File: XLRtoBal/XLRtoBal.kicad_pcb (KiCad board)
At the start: 2 copper layers, 53 parts, among them J1 XLR3, J10 Conn_Coaxial, J11 Conn_Coaxial, J2 Conn_01x04, J3 Conn_01x04, J4 XLR3, J5 Conn_01x04, J6 Conn_01x01, J7 Conn_01x01, J8 Conn_01x01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

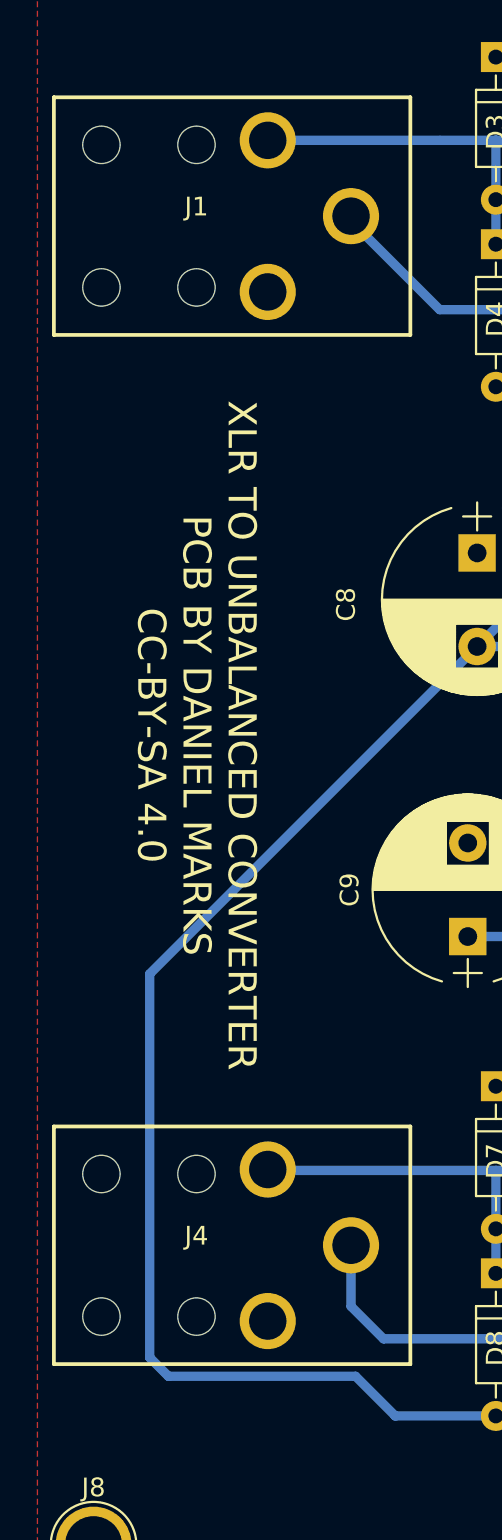
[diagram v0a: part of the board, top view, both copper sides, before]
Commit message: Fixed XLR footprint
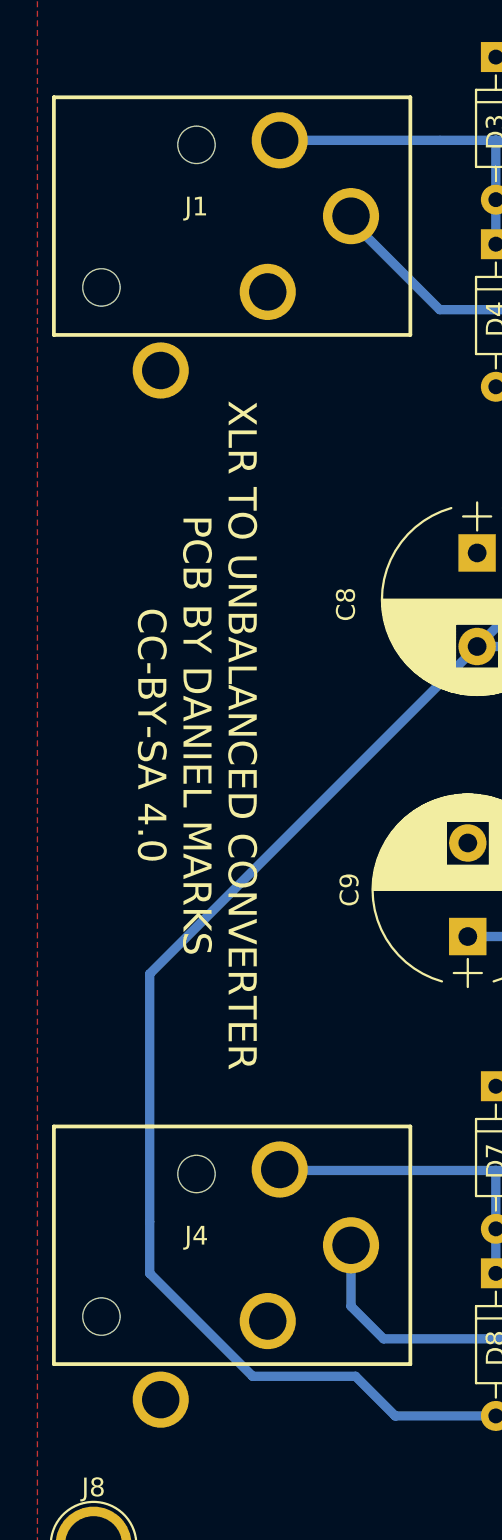
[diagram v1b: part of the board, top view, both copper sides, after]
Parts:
- J1, J4: footprint XLRtoBal:XLR04WP -> XLRtoBal:IOXLR3FEH
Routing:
- net VEE: track 177.5 -> 174.9 mm
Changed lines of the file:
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@@
     (thickness 1.6)
     (drawings 17)
-    (tracks 216)
+    (tracks 217)
     (zones 0)
     (modules 53)
@@
     (pad_to_mask_clearance 0.2)
     (aux_axis_origin 0 0)
-    (visible_elements FFFFFF7F)
+    (visible_elements 7FFFFFFF)
     (pcbplotparams
       (layerselection 0x00030_80000001)
@@
     )
   )
-  (module XLRtoBal:XLR04WP (layer F.Cu)
-    (at 110.5 78 180)
-    (fp_text reference J1 (at 0 0.5 180) (layer F.SilkS)
-      (effects (font (size 1 1) (thickness 0.15)))
-    )
-    (fp_text value XLR3 (at 0 -0.5 180) (layer F.Fab)
-      (effects (font (size 1 1) (thickness 0.15)))
-    )
-    (fp_line (start 7.62 -6.35) (end -11.43 -6.35) (layer F.SilkS) (width 0.2))
-    (fp_line (start -11.43 -6.35) (end -11.43 6.35) (layer F.SilkS) (width 0.2))
-    (fp_line (start -11.43 6.35) (end 7.62 6.35) (layer F.SilkS) (width 0.2))
-    (fp_line (start 7.62 6.35) (end 7.62 -6.35) (layer F.SilkS) (width 0.2))
-    (pad 3 thru_hole circle (at -8.26 0 180) (size 3 3) (drill 2) (layers *.Cu *.Mask)
-      (net 9 "Net-(D1-Pad2)"))
-    (pad 1 thru_hole circle (at -3.81 -4.05 180) (size 3 3) (drill 2) (layers *.Cu *.Mask)
-      (net 4 GND))
-    (pad "" np_thru_hole circle (at 0 -3.81 180) (size 2 2) (drill 2) (layers *.Cu *.Mask))
-    (pad "" np_thru_hole circle (at 5.08 3.81 180) (size 2 2) (drill 2) (layers *.Cu *.Mask))
-    (pad "" np_thru_hole circle (at 5.08 -3.81 180) (size 2 2) (drill 2) (layers *.Cu *.Mask))
-    (pad "" np_thru_hole circle (at 0 3.81 180) (size 2 2) (drill 2) (layers *.Cu *.Mask))
-    (pad 2 thru_hole circle (at -3.81 4.05 180) (size 3 3) (drill 2) (layers *.Cu *.Mask)
-      (net 12 "Net-(D3-Pad2)"))
-  )
   (module Connectors_Terminal_Blocks:TerminalBlock_bornier-4_P5.08mm (layer F.Cu)
     (at 176 62 270)
@@
       (rotate (xyz 0 0 0))
     )
-  )
-  (module XLRtoBal:XLR04WP (layer F.Cu)
-    (at 110.5 133 180)
-    (fp_text reference J4 (at 0 0.5 180) (layer F.SilkS)
-      (effects (font (size 1 1) (thickness 0.15)))
-    )
-    (fp_text value XLR3 (at 0 -0.5 180) (layer F.Fab)
-      (effects (font (size 1 1) (thickness 0.15)))
-    )
-    (fp_line (start 7.62 -6.35) (end -11.43 -6.35) (layer F.SilkS) (width 0.2))
-    (fp_line (start -11.43 -6.35) (end -11.43 6.35) (layer F.SilkS) (width 0.2))
-    (fp_line (start -11.43 6.35) (end 7.62 6.35) (layer F.SilkS) (width 0.2))
-    (fp_line (start 7.62 6.35) (end 7.62 -6.35) (layer F.SilkS) (width 0.2))
-    (pad 3 thru_hole circle (at -8.26 0 180) (size 3 3) (drill 2) (layers *.Cu *.Mask)
-      (net 21 "Net-(D10-Pad1)"))
-    (pad 1 thru_hole circle (at -3.81 -4.05 180) (size 3 3) (drill 2) (layers *.Cu *.Mask)
-      (net 4 GND))
-    (pad "" np_thru_hole circle (at 0 -3.81 180) (size 2 2) (drill 2) (layers *.Cu *.Mask))
-    (pad "" np_thru_hole circle (at 5.08 3.81 180) (size 2 2) (drill 2) (layers *.Cu *.Mask))
-    (pad "" np_thru_hole circle (at 5.08 -3.81 180) (size 2 2) (drill 2) (layers *.Cu *.Mask))
-    (pad "" np_thru_hole circle (at 0 3.81 180) (size 2 2) (drill 2) (layers *.Cu *.Mask))
-    (pad 2 thru_hole circle (at -3.81 4.05 180) (size 3 3) (drill 2) (layers *.Cu *.Mask)
-      (net 20 "Net-(D7-Pad2)"))
   )
   (module Connectors_Terminal_Blocks:TerminalBlock_bornier-4_P5.08mm (layer F.Cu)
@@
       (net 23 "Net-(J11-Pad1)"))
   )
+  (module XLRtoBal:IOXLR3FEH (layer F.Cu)
+    (at 110.5 78 180)
+    (fp_text reference J1 (at 0 0.5 180) (layer F.SilkS)
+      (effects (font (size 1 1) (thickness 0.15)))
+    )
+    (fp_text value XLR3 (at 0 -0.5 180) (layer F.Fab)
+      (effects (font (size 1 1) (thickness 0.15)))
+    )
+    (fp_line (start 7.62 -6.35) (end -11.43 -6.35) (layer F.SilkS) (width 0.2))
+    (fp_line (start -11.43 -6.35) (end -11.43 6.35) (layer F.SilkS) (width 0.2))
+    (fp_line (start -11.43 6.35) (end 7.62 6.35) (layer F.SilkS) (width 0.2))
+    (fp_line (start 7.62 6.35) (end 7.62 -6.35) (layer F.SilkS) (width 0.2))
+    (pad 3 thru_hole circle (at -8.26 0 180) (size 3 3) (drill 2) (layers *.Cu *.Mask)
+      (net 9 "Net-(D1-Pad2)"))
+    (pad 1 thru_hole circle (at -3.81 -4.05 180) (size 3 3) (drill 2) (layers *.Cu *.Mask)
+      (net 4 GND))
+    (pad "" np_thru_hole circle (at 5.08 -3.81 180) (size 2 2) (drill 2) (layers *.Cu *.Mask))
+    (pad "" np_thru_hole circle (at 0 3.81 180) (size 2 2) (drill 2) (layers *.Cu *.Mask))
+    (pad 2 thru_hole circle (at -4.45 4.05 180) (size 3 3) (drill 2) (layers *.Cu *.Mask)
+      (net 12 "Net-(D3-Pad2)"))
+    (pad G thru_hole circle (at 1.91 -8.25 180) (size 3 3) (drill 2) (layers *.Cu *.Mask))
+  )
+  (module XLRtoBal:IOXLR3FEH (layer F.Cu)
+    (at 110.5 133 180)
+    (fp_text reference J4 (at 0 0.5 180) (layer F.SilkS)
+      (effects (font (size 1 1) (thickness 0.15)))
+    )
+    (fp_text value XLR3 (at 0 -0.5 180) (layer F.Fab)
+      (effects (font (size 1 1) (thickness 0.15)))
+    )
+    (fp_line (start 7.62 -6.35) (end -11.43 -6.35) (layer F.SilkS) (width 0.2))
+    (fp_line (start -11.43 -6.35) (end -11.43 6.35) (layer F.SilkS) (width 0.2))
+    (fp_line (start -11.43 6.35) (end 7.62 6.35) (layer F.SilkS) (width 0.2))
+    (fp_line (start 7.62 6.35) (end 7.62 -6.35) (layer F.SilkS) (width 0.2))
+    (pad 3 thru_hole circle (at -8.26 0 180) (size 3 3) (drill 2) (layers *.Cu *.Mask)
+      (net 21 "Net-(D10-Pad1)"))
+    (pad 1 thru_hole circle (at -3.81 -4.05 180) (size 3 3) (drill 2) (layers *.Cu *.Mask)
+      (net 4 GND))
+    (pad "" np_thru_hole circle (at 5.08 -3.81 180) (size 2 2) (drill 2) (layers *.Cu *.Mask))
+    (pad "" np_thru_hole circle (at 0 3.81 180) (size 2 2) (drill 2) (layers *.Cu *.Mask))
+    (pad 2 thru_hole circle (at -4.45 4.05 180) (size 3 3) (drill 2) (layers *.Cu *.Mask)
+      (net 20 "Net-(D7-Pad2)"))
+    (pad G thru_hole circle (at 1.91 -8.25 180) (size 3 3) (drill 2) (layers *.Cu *.Mask))
+  )
   (gr_text "XLR TO UNBALANCED CONVERTER\nPCB BY DANIEL MARKS\nCC-BY-SA 4.0" (at 110.5 105.75 270) (layer F.SilkS)
     (effects (font (size 1.5 1.5) (thickness 0.3)))
@@
   (segment (start 140.5 83) (end 142 83) (width 0.5) (layer B.Cu) (net 3))
   (segment (start 142 83) (end 144 85) (width 0.5) (layer B.Cu) (net 3))
+  (segment (start 108 131.75) (end 108 134.5) (width 0.5) (layer B.Cu) (net 5))
+  (segment (start 108 134.5) (end 113.5 140) (width 0.5) (layer B.Cu) (net 5))
   (segment (start 126.5 142.12) (end 121.12 142.12) (width 0.5) (layer B.Cu) (net 5))
+  (segment (start 121.12 142.12) (end 119 140) (width 0.5) (layer B.Cu) (net 5))
+  (segment (start 119 140) (end 113.5 140) (width 0.5) (layer B.Cu) (net 5))
   (segment (start 108 118.5) (end 125.5 101) (width 0.5) (layer B.Cu) (net 5))
-  (segment (start 108 139) (end 108 118.5) (width 0.5) (layer B.Cu) (net 5))
-  (segment (start 109 140) (end 108 139) (width 0.5) (layer B.Cu) (net 5))
-  (segment (start 119 140) (end 109 140) (width 0.5) (layer B.Cu) (net 5))
-  (segment (start 121.12 142.12) (end 119 140) (width 0.5) (layer B.Cu) (net 5))
+  (segment (start 108 131.75) (end 108 118.5) (width 0.5) (layer B.Cu) (net 5))
   (segment (start 153 140.62) (end 151.88 140.62) (width 0.5) (layer B.Cu) (net 5))
   (segment (start 151.88 140.62) (end 150.5 142) (width 0.5) (layer B.Cu) (net 5))

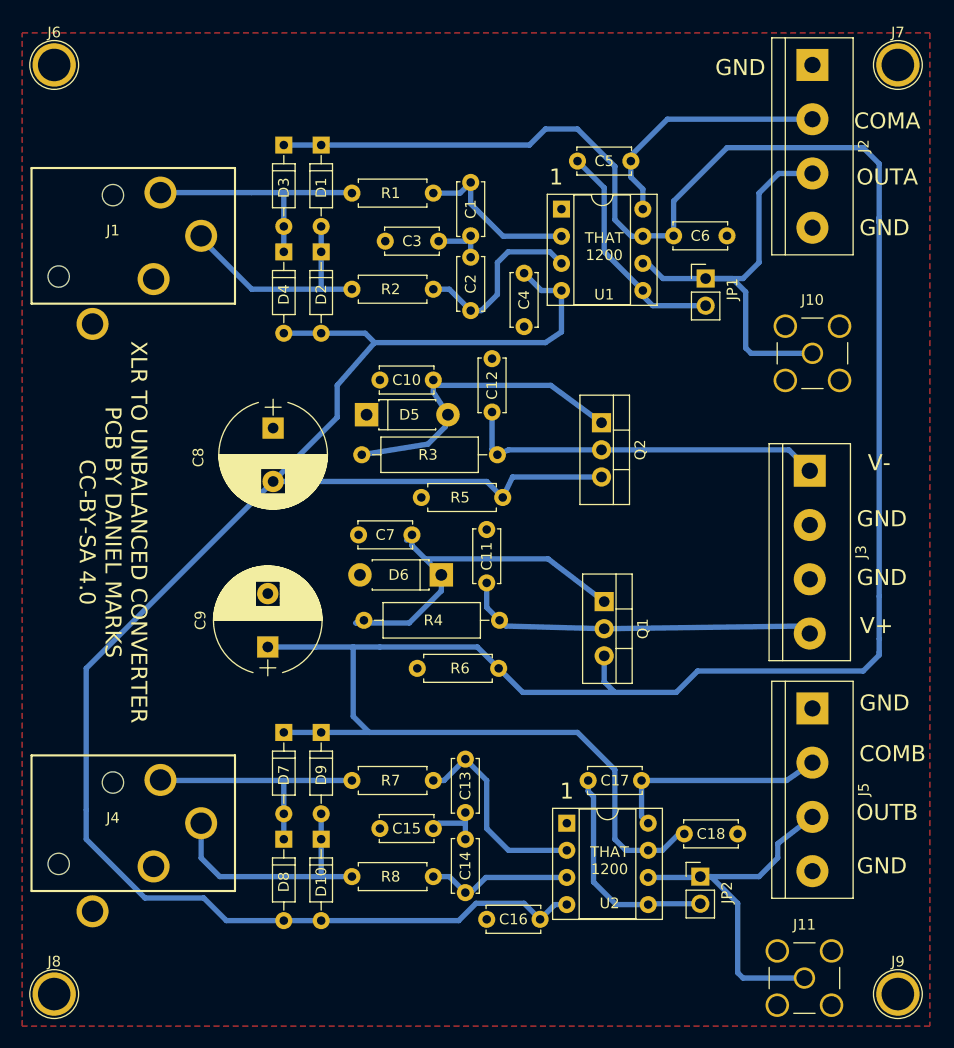
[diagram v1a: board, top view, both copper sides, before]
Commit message: Changed bootstrap capacitor
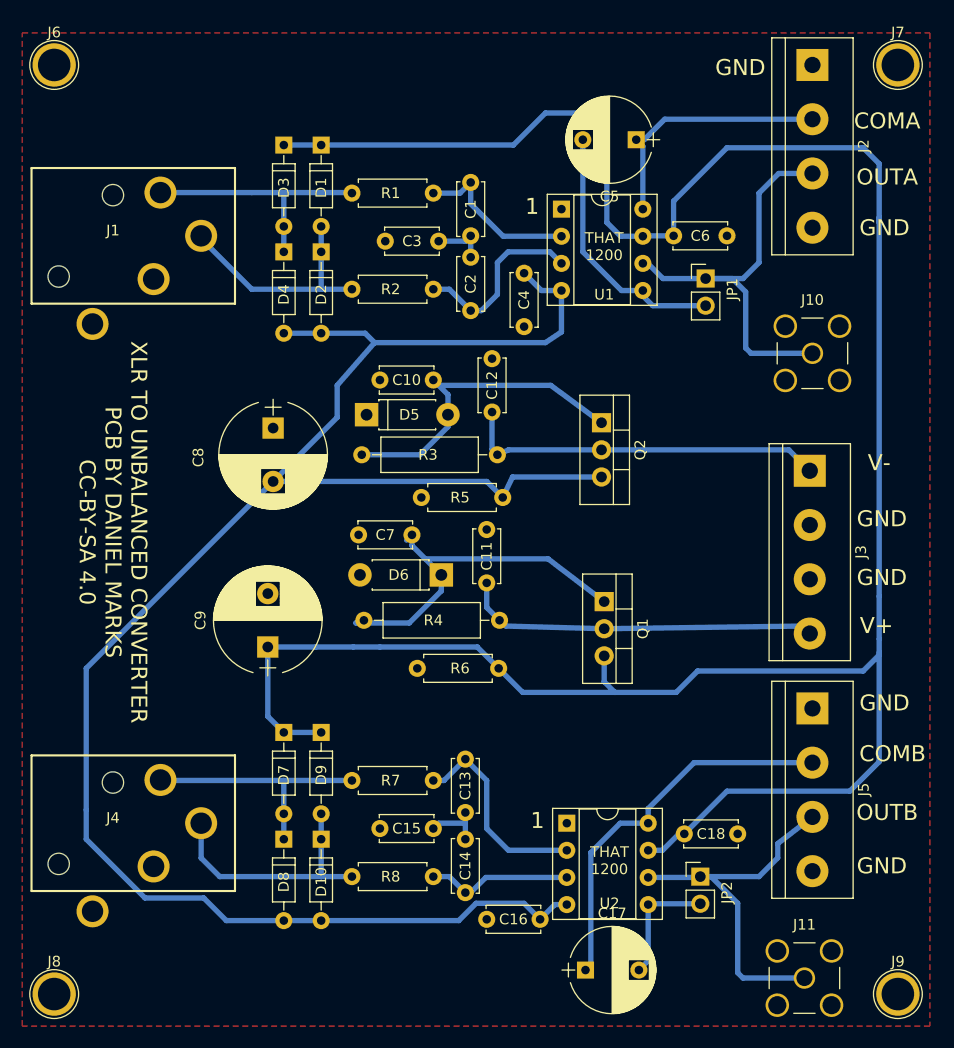
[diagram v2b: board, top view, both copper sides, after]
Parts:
- C17, C5: value CB -> 220 uF; footprint Capacitors_THT:C_Disc_D5.0mm_W2.5mm_P5.00mm -> Capacitors_THT:CP_Radial_D8.0mm_P5.00mm
- moved C17 17.8 mm to (154.8, 146.8)
- moved C5 5.85 mm to (159.5, 69.0), turned to 180 degrees
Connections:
- J2 pad 2: Net-(C5-Pad2) -> Net-(C5-Pad1)
- J5 pad 2: Net-(C17-Pad2) -> Net-(C17-Pad1)
- JP1 pad 2: Net-(C5-Pad1) -> Net-(C5-Pad2)
- JP2 pad 2: Net-(C17-Pad1) -> Net-(C17-Pad2)
- U1 pad 5: Net-(C5-Pad1) -> Net-(C5-Pad2)
- U1 pad 8: Net-(C5-Pad2) -> Net-(C5-Pad1)
- U2 pad 5: Net-(C17-Pad1) -> Net-(C17-Pad2)
- U2 pad 8: Net-(C17-Pad2) -> Net-(C17-Pad1)
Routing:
- net Net-(C17-Pad1): track 20.6 -> 37.0 mm
- net Net-(C17-Pad2): track 21.5 -> 11.4 mm
- net VCC: track 236.1 -> 231.7 mm
- net Net-(C5-Pad1): track 21.4 -> 24.1 mm
- net Net-(C10-Pad1): track 31.5 -> 32.7 mm
- net Net-(C5-Pad2): track 23.9 -> 24.4 mm

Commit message: Added soft start circuit
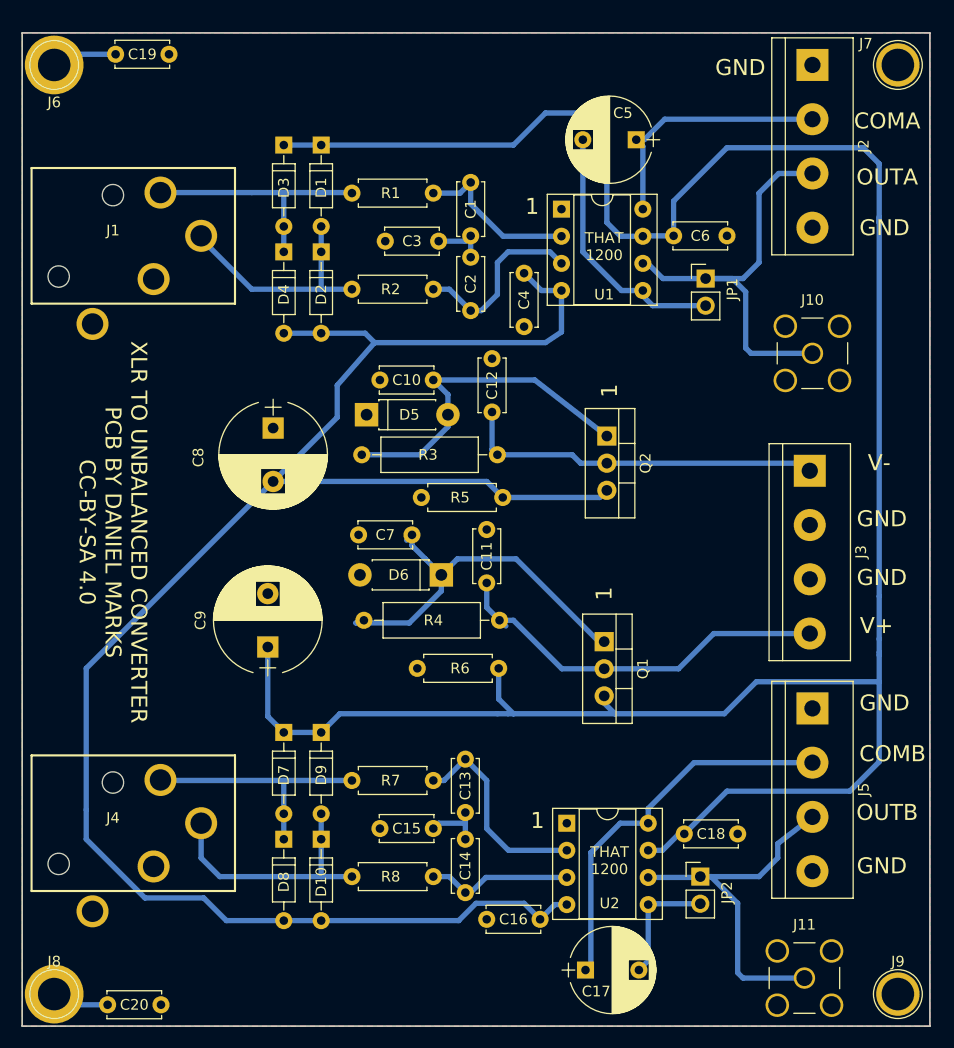
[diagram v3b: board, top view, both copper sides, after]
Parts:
- added C19: 100 nF, Capacitors_THT:C_Disc_D5.0mm_W2.5mm_P5.00mm, F.Cu at (110.8, 61.0)
- added C20: 100 nF, Capacitors_THT:C_Disc_D5.0mm_W2.5mm_P5.00mm, F.Cu at (110.0, 150.0)
- moved Q1 3.75 mm to (156.5, 116.0)
- moved Q2 1.35 mm to (156.8, 96.8)
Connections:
- J6 pad 1: (no net) -> Net-(C19-Pad1)
- J8 pad 1: (no net) -> Net-(C20-Pad1)
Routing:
- net Net-(C19-Pad1): track 0.00 -> 6.16 mm
- net Net-(C20-Pad1): track 0.00 -> 5.41 mm
- net Net-(C11-Pad2): track 33.9 -> 38.4 mm
- net VCC: track 231.7 -> 227.9 mm
- net Net-(C12-Pad1): track 34.4 -> 35.9 mm
- net Net-(C10-Pad1): track 32.7 -> 33.9 mm
- net Net-(C7-Pad2): track 35.2 -> 36.2 mm
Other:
- board outline added: 85 x 93 mm
